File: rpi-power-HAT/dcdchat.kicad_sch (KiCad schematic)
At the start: 31 parts

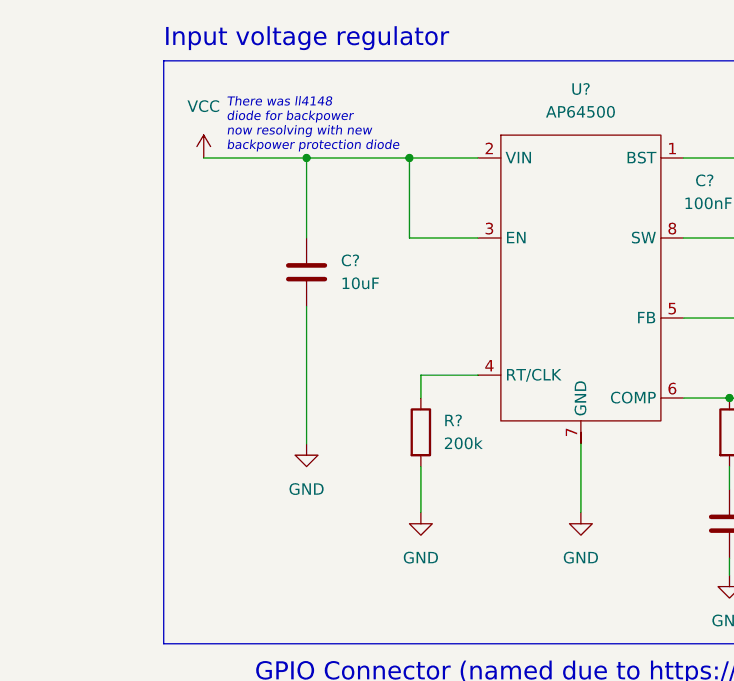
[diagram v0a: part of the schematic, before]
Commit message: Added backpower protection diode BSS84 before DC-DC
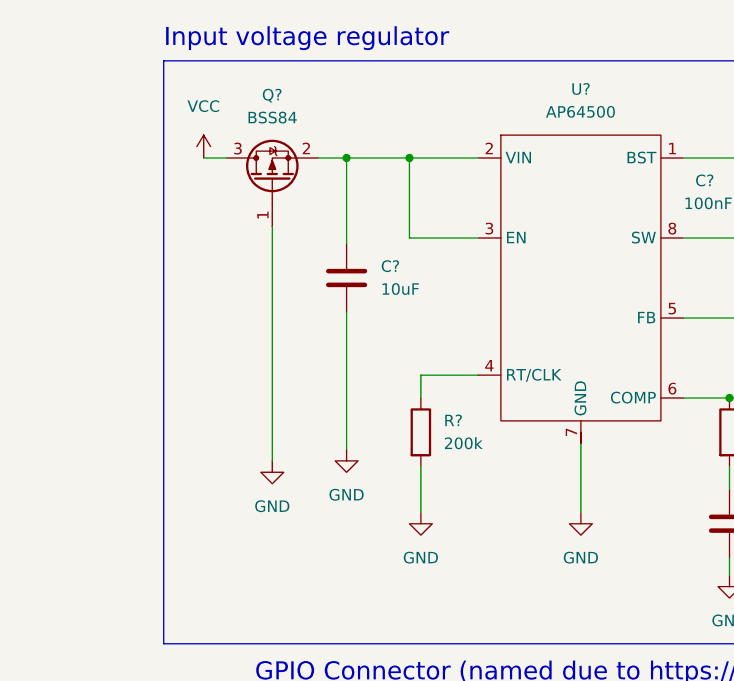
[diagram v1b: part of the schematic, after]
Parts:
- added Q?: BSS84, Package_TO_SOT_SMD:SOT-23, symbol Transistor_FET:BSS84
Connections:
- net GND: now also Q?.1 (G)
- net VCC: now also Q?.3 (D); no longer C?.1, U?.2 (VIN), U?.3 (EN)
- new net: C?.1, Q?.2 (S), U?.2 (VIN), U?.3 (EN)
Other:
- note removed: "There was ll4148 diode for backpower now resolving with new backpower protection diode"
- moved on the sheet: C?
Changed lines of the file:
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@@
   (junction (at 59.055 124.46) (diameter 0) (color 0 0 0 0)
   )
-  (junction (at 32.385 28.575) (diameter 0) (color 0 0 0 0)
-  )
   (junction (at 111.125 45.085) (diameter 0) (color 0 0 0 0)
   )
@@
   (junction (at 43.815 28.575) (diameter 0) (color 0 0 0 0)
   )
+  (junction (at 36.83 28.575) (diameter 0) (color 0 0 0 0)
+  )
   (junction (at 99.695 37.465) (diameter 0) (color 0 0 0 0)
   )
@@
     (stroke (width 0) (type default) (color 0 0 0 0))
   )
+  (wire (pts (xy 28.575 36.195) (xy 28.575 62.23))
+    (stroke (width 0) (type default) (color 0 0 0 0))
+  )
+  (wire (pts (xy 36.83 28.575) (xy 36.83 38.1))
+    (stroke (width 0) (type default) (color 0 0 0 0))
+  )
   (wire (pts (xy 160.655 61.595) (xy 160.655 58.42))
     (stroke (width 0) (type default) (color 0 0 0 0))
@@
     (stroke (width 0) (type default) (color 0 0 0 0))
   )
-  (wire (pts (xy 20.955 28.575) (xy 32.385 28.575))
+  (wire (pts (xy 20.955 28.575) (xy 23.495 28.575))
     (stroke (width 0) (type default) (color 0 0 0 0))
   )
@@
     (stroke (width 0) (type default) (color 0 0 0 0))
   )
-  (wire (pts (xy 32.385 45.085) (xy 32.385 60.325))
+  (wire (pts (xy 36.83 45.72) (xy 36.83 60.96))
     (stroke (width 0) (type default) (color 0 0 0 0))
   )
@@
     (stroke (width 0) (type default) (color 0 0 0 0))
   )
-  (wire (pts (xy 32.385 28.575) (xy 43.815 28.575))
-    (stroke (width 0) (type default) (color 0 0 0 0))
-  )
   (wire (pts (xy 17.145 134.62) (xy 38.735 134.62))
     (stroke (width 0) (type default) (color 0 0 0 0))
@@
     (stroke (width 0) (type default) (color 0 0 0 0))
   )
-  (wire (pts (xy 32.385 28.575) (xy 32.385 37.465))
-    (stroke (width 0) (type default) (color 0 0 0 0))
-  )
   (wire (pts (xy 90.805 64.135) (xy 90.805 70.485))
     (stroke (width 0) (type default) (color 0 0 0 0))
@@
     (stroke (width 0) (type default) (color 0 0 0 0))
   )
+  (wire (pts (xy 33.655 28.575) (xy 36.83 28.575))
+    (stroke (width 0) (type default) (color 0 0 0 0))
+  )
   (wire (pts (xy 257.81 109.855) (xy 268.605 109.855))
     (stroke (width 0) (type default) (color 0 0 0 0))
@@
   )
   (polyline (pts (xy 239.395 62.865) (xy 239.395 92.71))
+    (stroke (width 0) (type default) (color 0 0 0 0))
+  )
+  (wire (pts (xy 36.83 28.575) (xy 43.815 28.575))
     (stroke (width 0) (type default) (color 0 0 0 0))
   )
@@
   (text "UART connector 2" (at 240.03 61.595 0)
     (effects (font (size 2 2)) (justify left bottom))
-  )
-  (text "There was ll4148 \ndiode for backpower \nnow resolving with new \nbackpower protection diode"
-    (at 23.495 27.94 0)
-    (effects (font (size 1 1) italic) (justify left bottom))
   )
   (text "Level converter\n(5V to 3.3V)" (at 214.63 23.495 0)
@@
     (pin "1")
   )
+  (symbol (lib_id "power:GND") (at 28.575 62.23 0) (unit 1)
+    (in_bom yes) (on_board yes) (fields_autoplaced)
+    (property "Reference" "#PWR?" (id 0) (at 28.575 68.58 0)
+      (effects (font (size 1.27 1.27)) hide)
+    )
+    (property "Value" "GND" (id 1) (at 28.575 67.31 0))
+    (property "Footprint" "" (id 2) (at 28.575 62.23 0)
+      (effects (font (size 1.27 1.27)) hide)
+    )
+    (property "Datasheet" "" (id 3) (at 28.575 62.23 0)
+      (effects (font (size 1.27 1.27)) hide)
+    )
+    (pin "1")
+  )
   (symbol (lib_id "power:GND") (at 220.345 65.405 0) (unit 1)
     (in_bom yes) (on_board yes) (fields_autoplaced)
@@
     (pin "1")
   )
-  (symbol (lib_id "Device:C") (at 32.385 41.275 0) (unit 1)
-    (in_bom yes) (on_board yes) (fields_autoplaced)
-    (property "Reference" "C?" (id 0) (at 36.195 40.0049 0)
-      (effects (font (size 1.27 1.27)) (justify left))
-    )
-    (property "Value" "10uF" (id 1) (at 36.195 42.5449 0)
-      (effects (font (size 1.27 1.27)) (justify left))
-    )
-    (property "Footprint" "" (id 2) (at 33.3502 45.085 0)
-      (effects (font (size 1.27 1.27)) hide)
-    )
-    (property "Datasheet" "~" (id 3) (at 32.385 41.275 0)
+  (symbol (lib_id "Device:C") (at 36.83 41.91 0) (unit 1)
+    (in_bom yes) (on_board yes) (fields_autoplaced)
+    (property "Reference" "C?" (id 0) (at 40.64 40.6399 0)
+      (effects (font (size 1.27 1.27)) (justify left))
+    )
+    (property "Value" "10uF" (id 1) (at 40.64 43.1799 0)
+      (effects (font (size 1.27 1.27)) (justify left))
+    )
+    (property "Footprint" "" (id 2) (at 37.7952 45.72 0)
+      (effects (font (size 1.27 1.27)) hide)
+    )
+    (property "Datasheet" "~" (id 3) (at 36.83 41.91 0)
       (effects (font (size 1.27 1.27)) hide)
     )
@@
     )
     (pin "1")
+  )
+  (symbol (lib_id "Transistor_FET:BSS84") (at 28.575 31.115 90) (unit 1)
+    (in_bom yes) (on_board yes) (fields_autoplaced)
+    (property "Reference" "Q?" (id 0) (at 28.575 21.59 90))
+    (property "Value" "BSS84" (id 1) (at 28.575 24.13 90))
+    (property "Footprint" "Package_TO_SOT_SMD:SOT-23" (id 2) (at 30.48 26.035 0)
+      (effects (font (size 1.27 1.27) italic) (justify left) hide)
+    )
+    (property "Datasheet" "http://assets.nexperia.com/documents/data-sheet/BSS84.pdf" (id 3) (at 28.575 31.115 0)
+      (effects (font (size 1.27 1.27)) (justify left) hide)
+    )
+    (pin "1")
+    (pin "2")
+    (pin "3")
   )
   (symbol (lib_id "power:GND") (at 62.865 67.945 0) (unit 1)
@@
     (pin "2")
   )
-  (symbol (lib_id "power:GND") (at 32.385 60.325 0) (unit 1)
-    (in_bom yes) (on_board yes) (fields_autoplaced)
-    (property "Reference" "#PWR?" (id 0) (at 32.385 66.675 0)
-      (effects (font (size 1.27 1.27)) hide)
-    )
-    (property "Value" "GND" (id 1) (at 32.385 65.405 0))
-    (property "Footprint" "" (id 2) (at 32.385 60.325 0)
-      (effects (font (size 1.27 1.27)) hide)
-    )
-    (property "Datasheet" "" (id 3) (at 32.385 60.325 0)
+  (symbol (lib_id "power:GND") (at 36.83 60.96 0) (unit 1)
+    (in_bom yes) (on_board yes) (fields_autoplaced)
+    (property "Reference" "#PWR?" (id 0) (at 36.83 67.31 0)
+      (effects (font (size 1.27 1.27)) hide)
+    )
+    (property "Value" "GND" (id 1) (at 36.83 66.04 0))
+    (property "Footprint" "" (id 2) (at 36.83 60.96 0)
+      (effects (font (size 1.27 1.27)) hide)
+    )
+    (property "Datasheet" "" (id 3) (at 36.83 60.96 0)
       (effects (font (size 1.27 1.27)) hide)
     )
@@
       (reference "#PWR?") (unit 1) (value "GND") (footprint "")
     )
+    (path "/7a07c9aa-388b-4f56-99da-65b2a636d77f"
+      (reference "#PWR?") (unit 1) (value "GND") (footprint "")
+    )
     (path "/7ab600a3-244e-43f2-ade1-8eda2d231ce6"
       (reference "#PWR?") (unit 1) (value "GND") (footprint "")
@@
       (reference "Q?") (unit 1) (value "DMG2305UX") (footprint "")
     )
+    (path "/a61875d9-72de-4986-ae1b-1b43bcf6afea"
+      (reference "Q?") (unit 1) (value "BSS84") (footprint "Package_TO_SOT_SMD:SOT-23")
+    )
     (path "/38721968-4ada-4274-b60a-135c2cb78357"

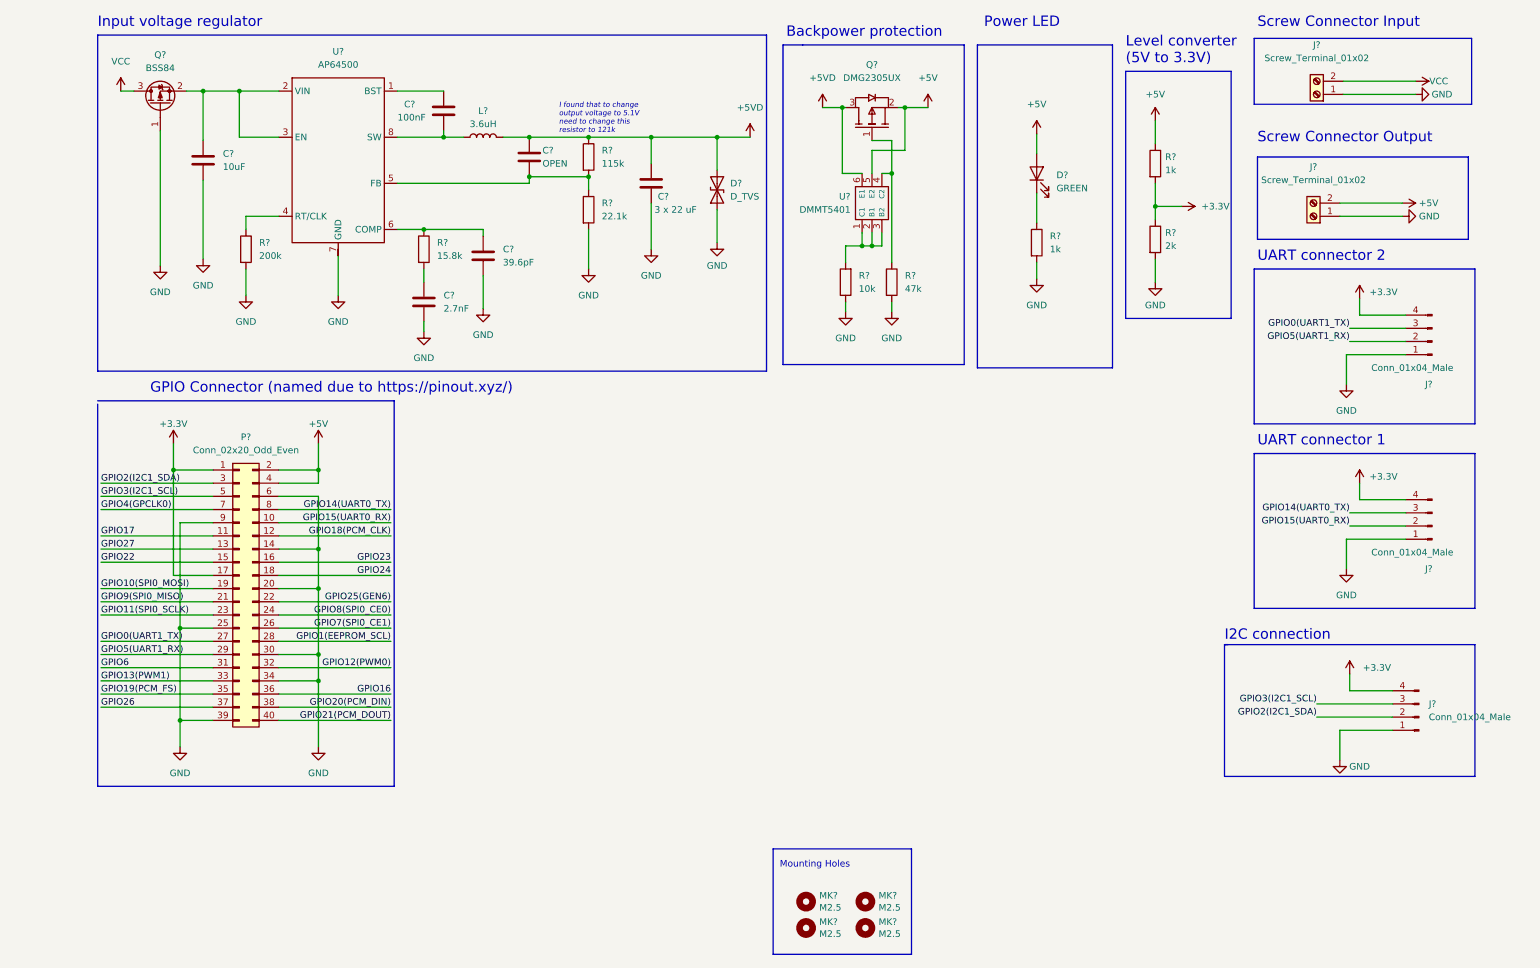
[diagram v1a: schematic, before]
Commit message: made changes due to  28.11.2024 message
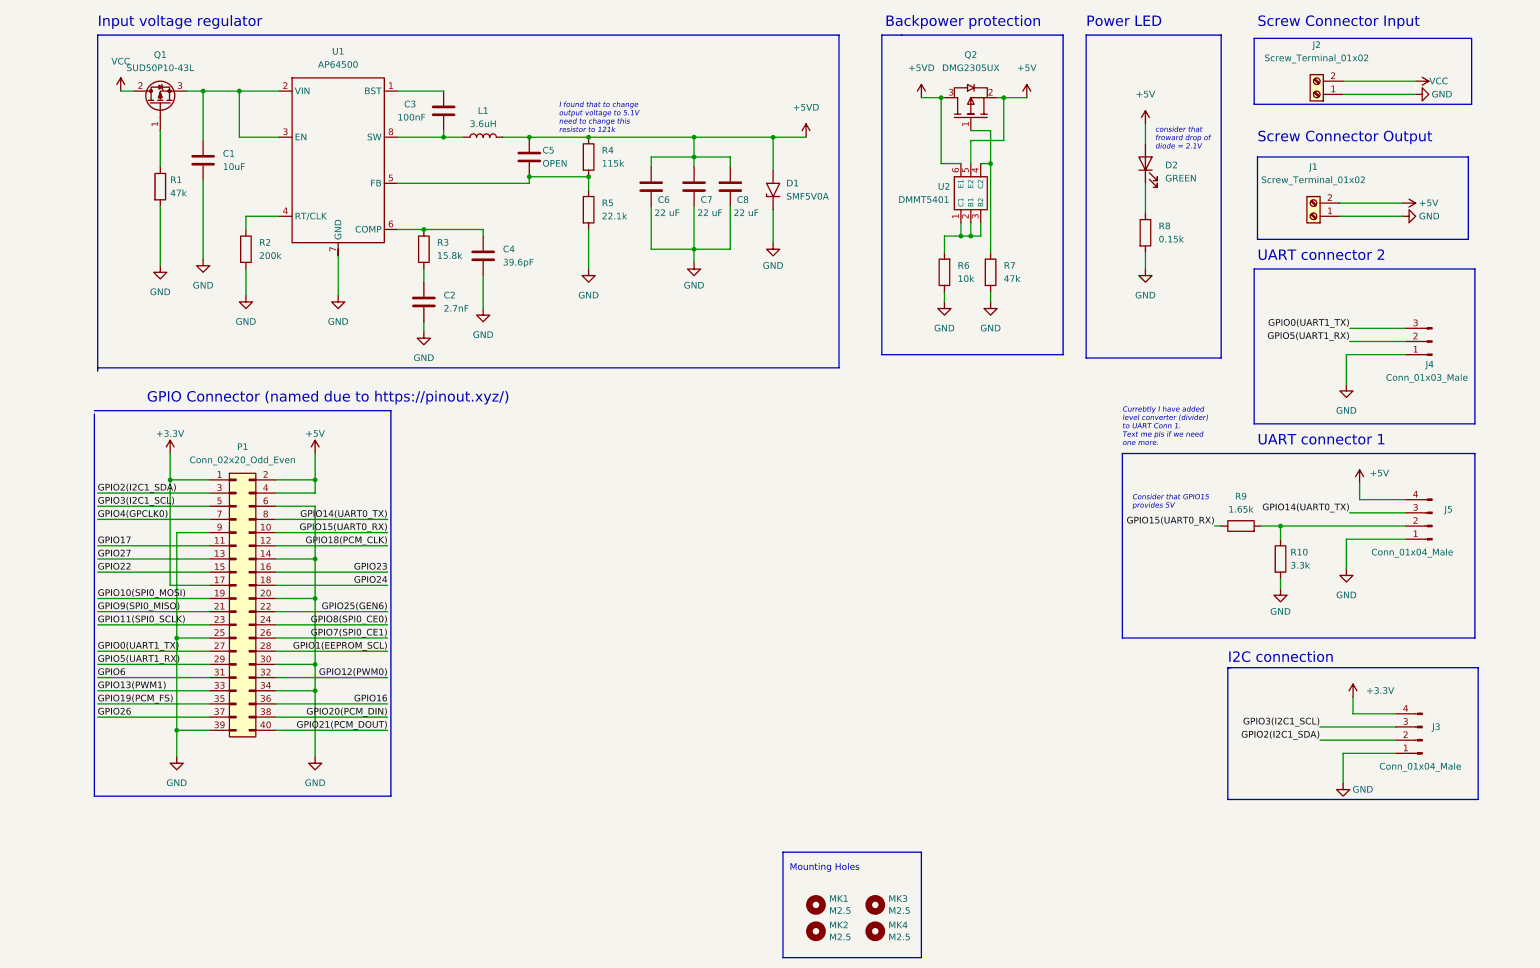
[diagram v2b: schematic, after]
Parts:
- removed D?: D_TVS, symbol Device:D_TVS
- removed J?: Conn_01x04_Male, symbol Connector:Conn_01x04_Male
- removed Q?: BSS84, Package_TO_SOT_SMD:SOT-23, symbol Transistor_FET:BSS84
- added C7, C8: 22 uF, symbol Device:C
- added D1: SMF5V0A, Diode_SMD:D_SMF, symbol Diode:SMF5V0A
- added J4: Conn_01x03_Male, Connector_JST:JST_PH_B3B-PH-K_1x03_P2.00mm_Vertical, symbol Connector:Conn_01x03_Male
- added Q1: SUD50P10-43L, Package_TO_SOT_SMD:TO-252-2, symbol Transistor_FET:SUD50P10-43L
- added R1: 47k, symbol Device:R
- C6: renamed from C?; value 3 x 22 uF -> 22 uF
- J3, J5: renamed from J?; footprint (none) -> Connector_JST:JST_PH_B4B-PH-K_1x04_P2.00mm_Vertical
- Q2: renamed from Q?; footprint (none) -> ultralibDMG2305UX:DMG2305UX-7
- R10: renamed from R?; value 2k -> 3.3k
- R8: renamed from R?; value 1k -> 0.15k
- R9: renamed from R?; value 1k -> 1.65k
- U1: renamed from U?; footprint (none) -> ultralibAP64500:AP64500SP-13
- U2: renamed from U?; footprint (none) -> ultralibDMG2305UX:DMG2305UX-7
- gave numbers to parts that had none: 20
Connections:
- net +3.3V: no longer J5.4 (Pin_4), R10.1, R9.2
- net +5V: now also J5.4 (Pin_4); no longer R9.1
- net +5VD: now also C7.1, C8.1, D1.2 (A2)
- net GND: now also C7.2, C8.2, D1.1 (A1), J4.1 (Pin_1), R1.2
- net GPIO0(UART1_TX): now also J4.3 (Pin_3)
- net GPIO15(UART0_RX): now also R9.1; no longer J5.2 (Pin_2)
- net GPIO5(UART1_RX): now also J4.2 (Pin_2)
- net VCC: now also Q1.2 (D)
- net at C1.1, U1.2 (VIN), U1.3 (EN): now also Q1.3 (S)
- new net: Q1.1 (G), R1.1
- new net: J5.2 (Pin_2), R10.1, R9.2
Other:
- note added: "Consider that GPIO15 provides 5V"
- note added: "Currebtly I have added level converter (divider) to UART Conn 1. Text me pls if we need one more."
- note added: "consider that froward drop of diode = 2.1V"
- note removed: "Level converter (5V to 3.3V)"
- moved on the sheet: C6, D2, J3, MK1, MK2, MK3, MK4, P1, Q2, R10, R6, R7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

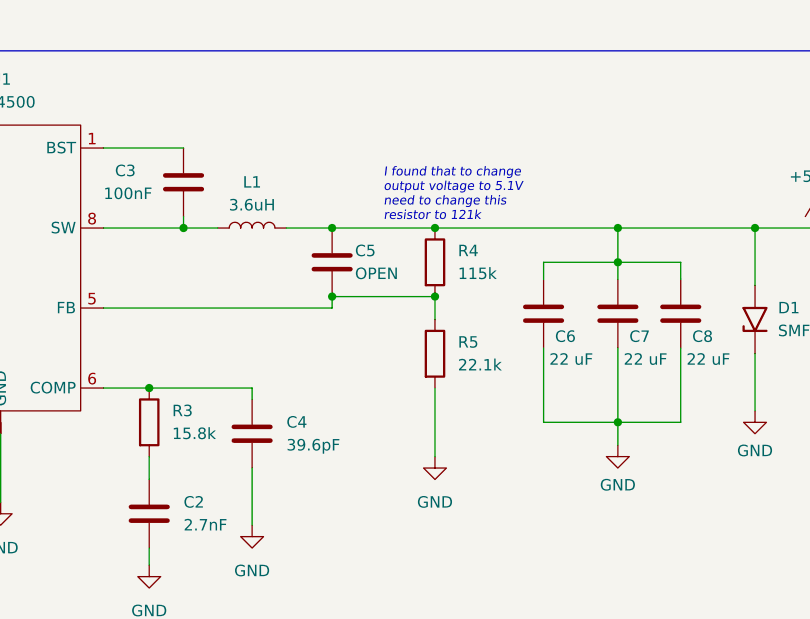
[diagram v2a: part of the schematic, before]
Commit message: DC-DC converter elements values changes
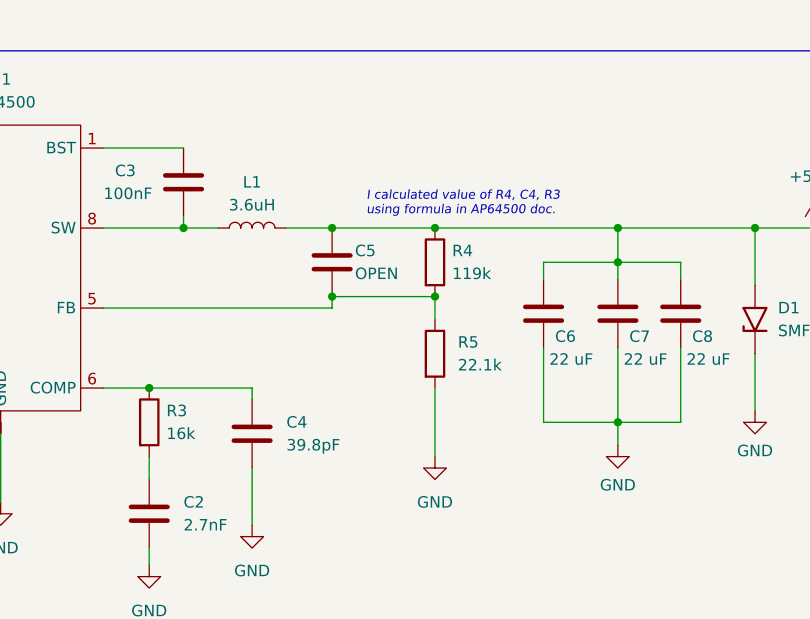
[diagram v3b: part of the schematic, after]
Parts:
- C4: value 39.6pF -> 39.8pF
- R3: value 15.8k -> 16k
- R4: value 115k -> 119k
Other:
- note added: "I calculated value of R4, C4, R3 using formula in AP64500 doc."
- note removed: "I found that to change output voltage to 5.1V need to change this resistor to 121k"
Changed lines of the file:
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@@
     (effects (font (size 2 2)) (justify left bottom))
   )
-  (text "I found that to change\noutput voltage to 5.1V\nneed to change this \nresistor to 121k"
-    (at 105.41 36.83 0)
+  (text "I calculated value of R4, C4, R3\nusing formula in AP64500 doc. \n"
+    (at 103.505 36.195 0)
     (effects (font (size 1 1) italic) (justify left bottom))
   )
@@
   (symbol (lib_id "Device:R") (at 111.125 41.275 0) (unit 1)
     (in_bom yes) (on_board yes) (fields_autoplaced)
-    (property "Reference" "R4" (id 0) (at 113.665 40.0049 0)
-      (effects (font (size 1.27 1.27)) (justify left))
-    )
-    (property "Value" "115k" (id 1) (at 113.665 42.5449 0)
+    (property "Reference" "R4" (id 0) (at 113.03 40.0049 0)
+      (effects (font (size 1.27 1.27)) (justify left))
+    )
+    (property "Value" "119k" (id 1) (at 113.03 42.5449 0)
       (effects (font (size 1.27 1.27)) (justify left))
     )
@@
       (effects (font (size 1.27 1.27)) (justify left))
     )
-    (property "Value" "39.6pF" (id 1) (at 94.615 61.5949 0)
+    (property "Value" "39.8pF" (id 1) (at 94.615 61.5949 0)
       (effects (font (size 1.27 1.27)) (justify left))
     )
@@
   (symbol (lib_id "Device:R") (at 79.375 59.055 0) (unit 1)
     (in_bom yes) (on_board yes) (fields_autoplaced)
-    (property "Reference" "R3" (id 0) (at 81.915 57.7849 0)
-      (effects (font (size 1.27 1.27)) (justify left))
-    )
-    (property "Value" "15.8k" (id 1) (at 81.915 60.3249 0)
+    (property "Reference" "R3" (id 0) (at 81.28 57.7849 0)
+      (effects (font (size 1.27 1.27)) (justify left))
+    )
+    (property "Value" "16k" (id 1) (at 81.28 60.3249 0)
       (effects (font (size 1.27 1.27)) (justify left))
     )
@@
     )
     (path "/a2d2f930-8739-4910-8da2-fdac6e010707"
-      (reference "C4") (unit 1) (value "39.6pF") (footprint "")
+      (reference "C4") (unit 1) (value "39.8pF") (footprint "")
     )
     (path "/546d44ff-42d4-46cb-9d91-74c808740184"
@@
     )
     (path "/c291683c-ab20-4c3b-a113-e9f5c41c36b8"
-      (reference "R3") (unit 1) (value "15.8k") (footprint "")
+      (reference "R3") (unit 1) (value "16k") (footprint "")
     )
     (path "/4b4c1b78-dbfd-4057-84d4-e5c010190612"
-      (reference "R4") (unit 1) (value "115k") (footprint "")
+      (reference "R4") (unit 1) (value "119k") (footprint "")
     )
     (path "/5ec5a876-af46-4cc2-8f4a-ae87a431be92"
